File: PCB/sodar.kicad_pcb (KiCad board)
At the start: 2 copper layers, 71 parts, among them J1 Screw_Terminal_01x02, J2 Conn_02x12_Counter_Clockwise, J3 Conn_01x02, U1 TC78H621FNG, U10 TC78H621FNG, U2 TC78H621FNG, U3 TC78H621FNG, U4 TC78H621FNG, U5 TC78H621FNG, U6 TC78H621FNG, U7 TC78H621FNG, U8 TC78H621FNG, U9 TC78H621FNG

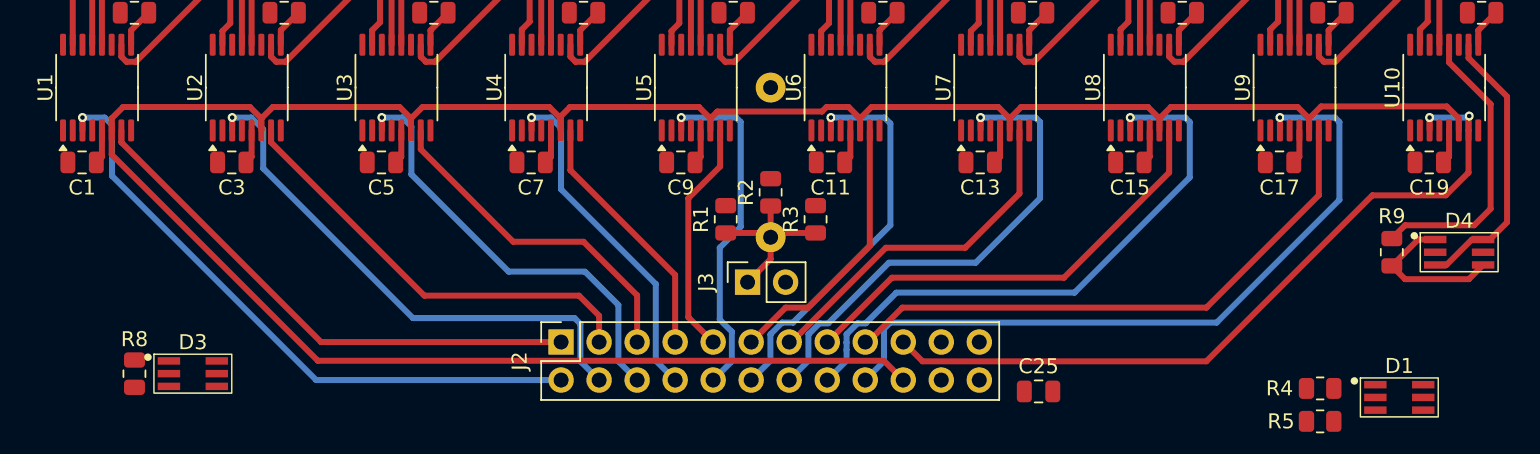
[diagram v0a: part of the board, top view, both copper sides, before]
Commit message: Better STBY routing & Started to route EN
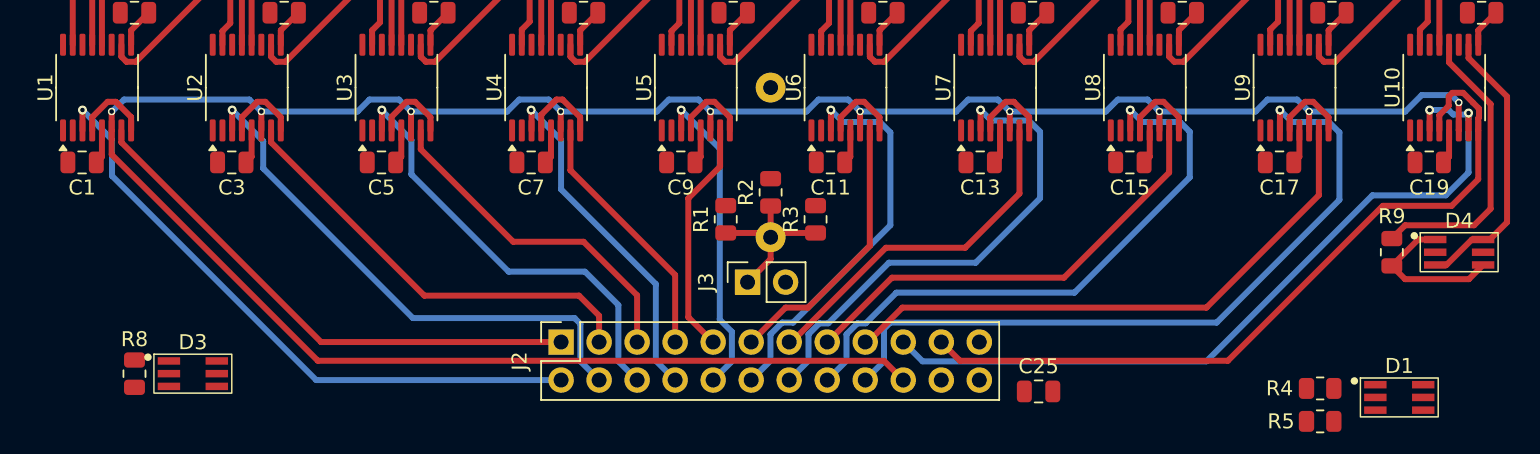
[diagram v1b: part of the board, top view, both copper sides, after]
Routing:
- net EN: track 0.00 -> 98.5 mm
- net STBY: track 165.3 -> 169.9 mm, vias 0 -> 10
- net S9: track 23.7 -> 21.3 mm
- net S19: track 50.9 -> 52.5 mm

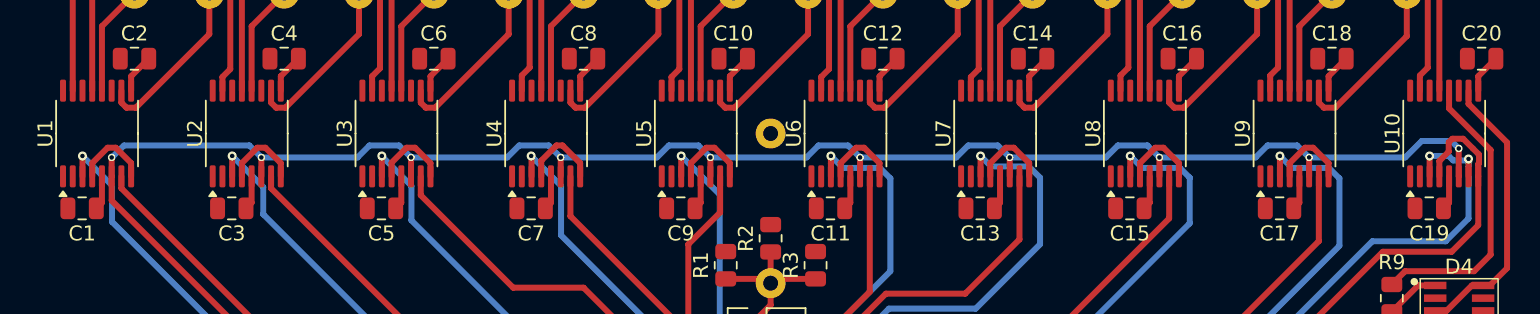
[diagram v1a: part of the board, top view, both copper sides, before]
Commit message: Routed EN
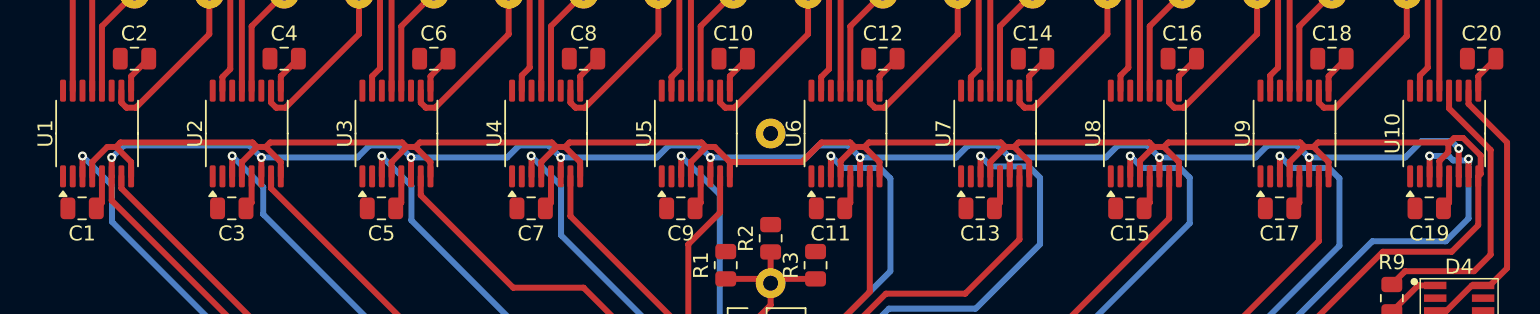
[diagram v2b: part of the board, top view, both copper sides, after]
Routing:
- net EN: track 98.5 -> 185.8 mm

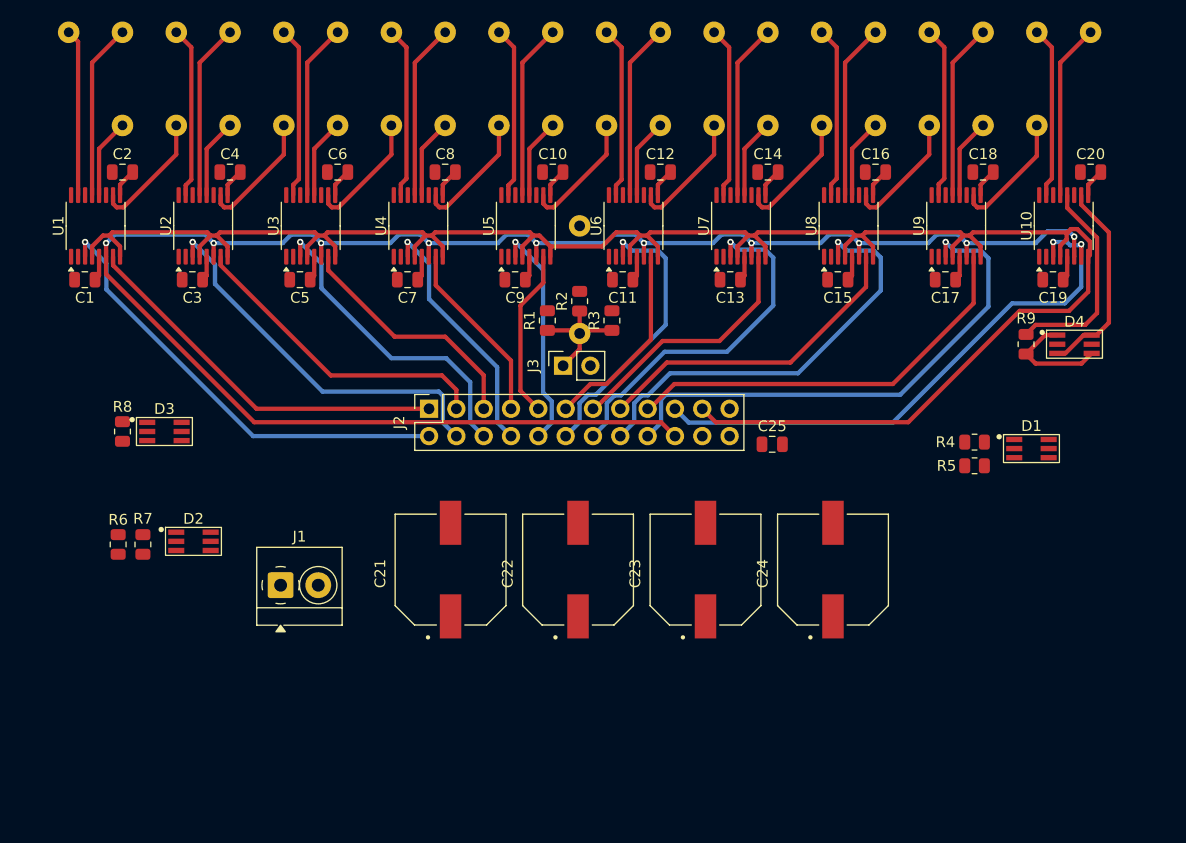
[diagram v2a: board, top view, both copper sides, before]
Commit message: Moved the header 2mm lower so that there is space for the receiver
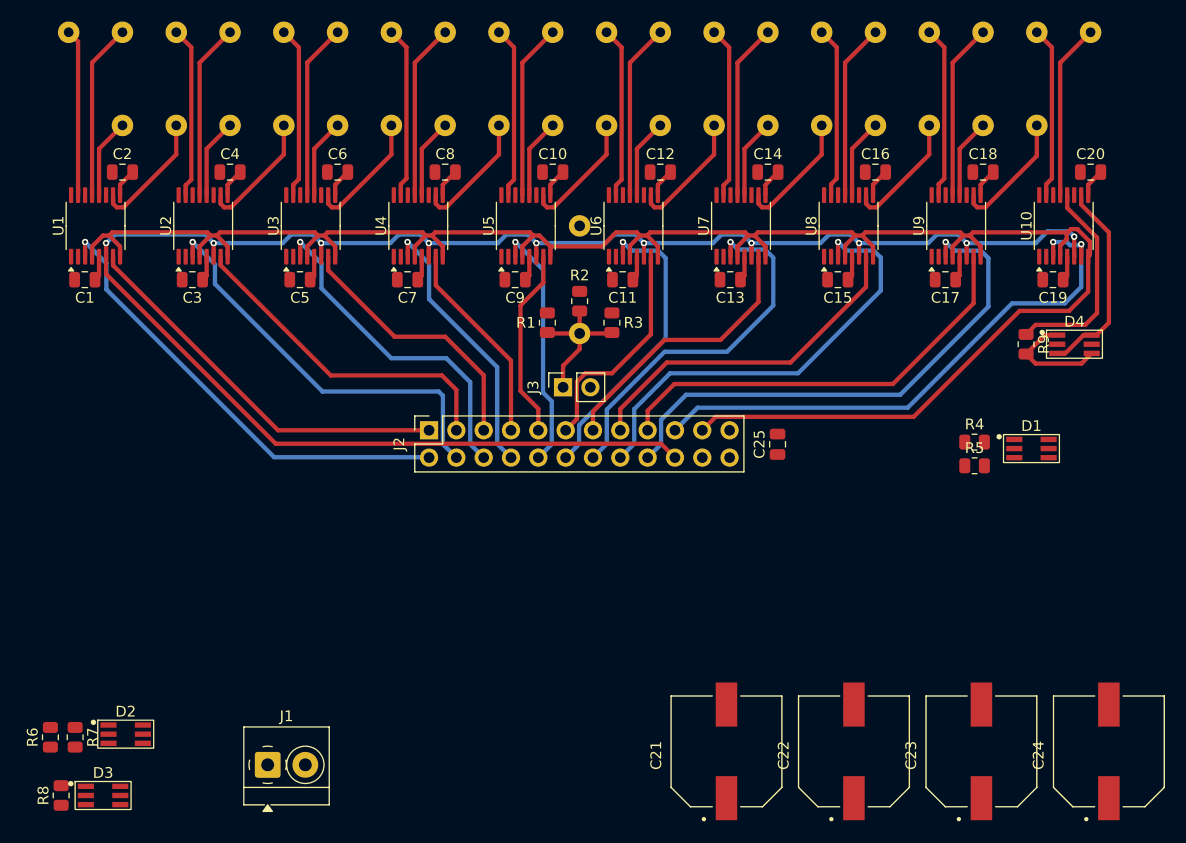
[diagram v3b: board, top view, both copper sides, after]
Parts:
- moved D3 34.3 mm to (105.7, 106.0)
- moved R8 34.3 mm to (101.8, 106.0)
- moved C21 30.7 mm to (163.7, 101.8)
- moved C22 30.7 mm to (175.5, 101.8)
- moved C23 30.7 mm to (187.3, 101.8)
- moved C24 30.7 mm to (199.2, 101.8)
- moved R7 19.0 mm to (103.1, 100.5)
- moved D2 19.0 mm to (107.8, 100.2)
- moved R6 19.0 mm to (100.8, 100.5)
- moved J1 16.7 mm to (121.0, 103.1)
- moved J2 2.00 mm to (136.0, 72.0)
- moved J3 2.00 mm to (148.5, 68.0)
- moved C25 0.50 mm to (168.4, 73.3), turned to 90 degrees
- moved R1 0.20 mm to (147.0, 62.0)
- moved R3 0.20 mm to (153.0, 62.0)
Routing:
- net S12: track 18.3 -> 20.9 mm
- net S5: track 29.3 -> 31.3 mm
- net S10: track 15.7 -> 17.7 mm
- net S9: track 21.3 -> 23.3 mm
- net S8: track 17.0 -> 19.0 mm
- net S6: track 22.9 -> 24.9 mm
- net S4: track 29.3 -> 31.3 mm
- net S3: track 35.9 -> 37.9 mm
- net S7: track 23.4 -> 25.4 mm
- net S16: track 30.3 -> 32.3 mm
- net S18: track 38.7 -> 40.6 mm
- net S14: track 23.7 -> 25.6 mm
- net RX: track 12.0 -> 13.8 mm
- net S15: track 39.9 -> 41.5 mm
- net S13: track 33.2 -> 34.9 mm
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
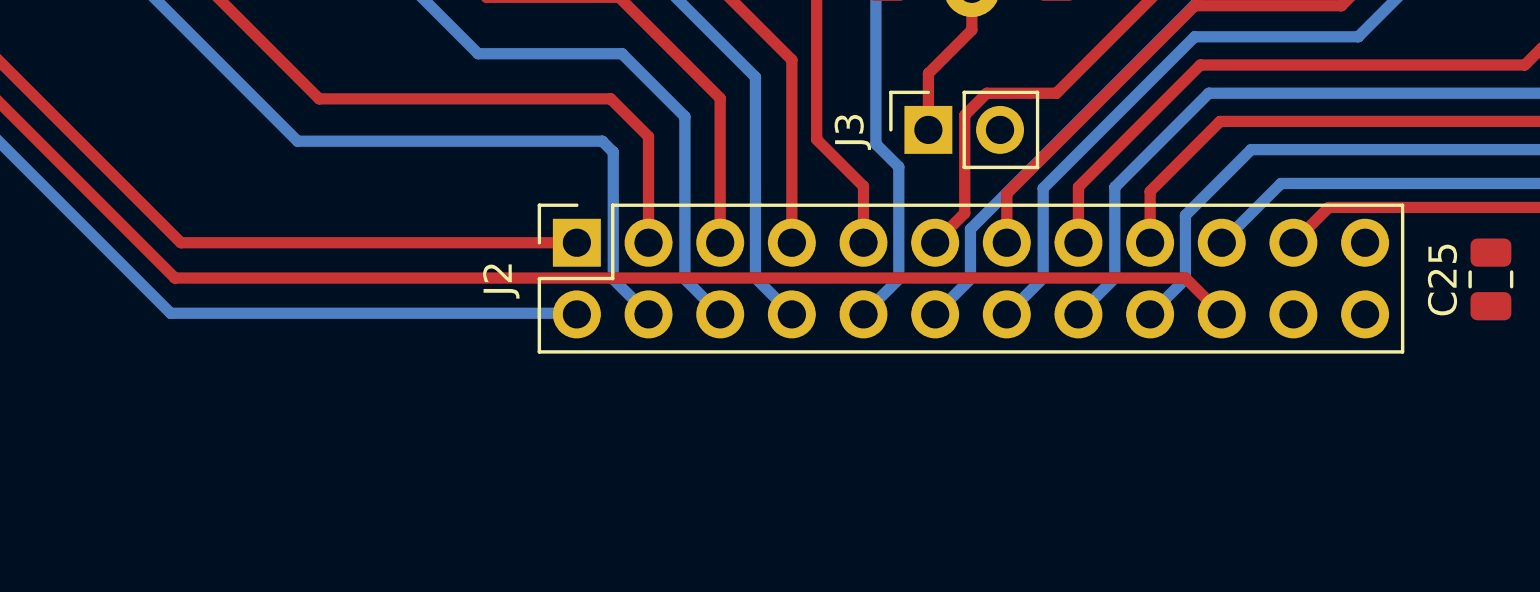
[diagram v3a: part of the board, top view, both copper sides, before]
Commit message: Rerouted STBY to 3V3 as we set it to 3V3 anyway
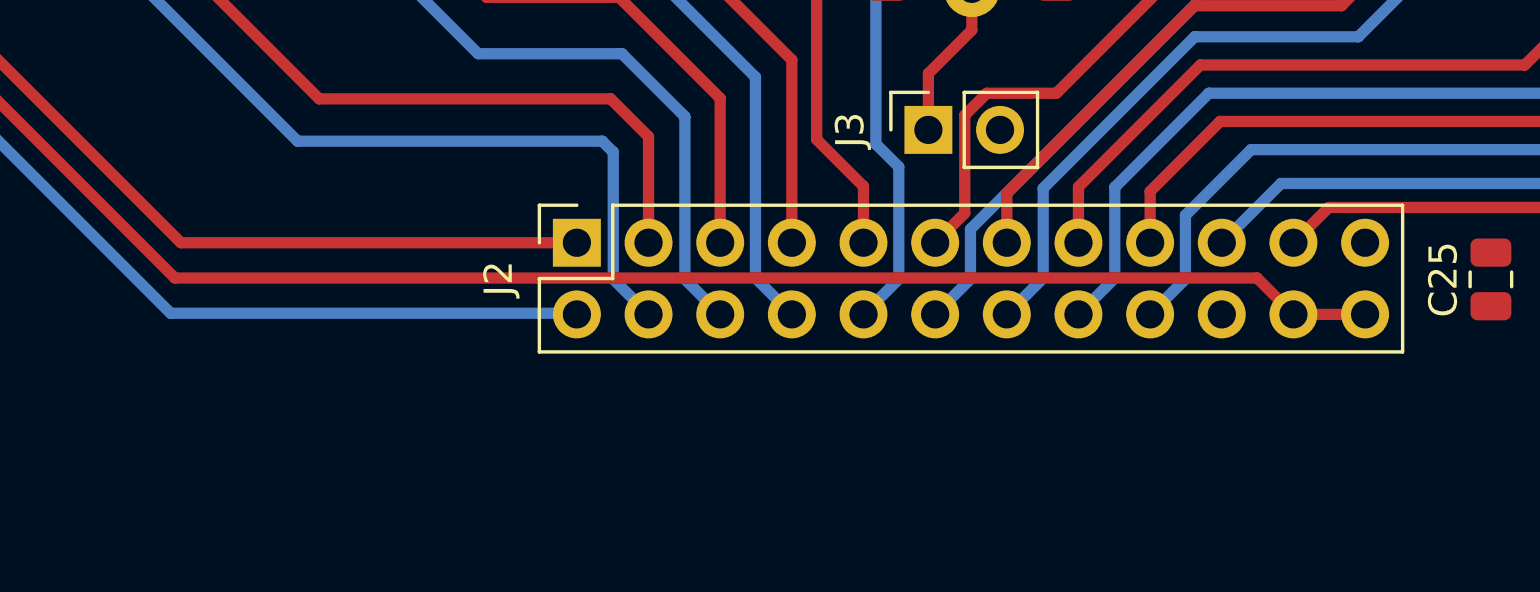
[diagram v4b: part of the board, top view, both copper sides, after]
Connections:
- D1 pad 6: STBY -> +3V3
- J2 pad 20: STBY -> LED
- J2 pad 22: LED -> +3V3
- U1 pad 6: STBY -> +3V3
- U10 pad 6: STBY -> +3V3
- U2 pad 6: STBY -> +3V3
- U3 pad 6: STBY -> +3V3
- U4 pad 6: STBY -> +3V3
- U5 pad 6: STBY -> +3V3
- U6 pad 2: S11 -> unconnected-(U6-NC-Pad2)
- U6 pad 6: STBY -> +3V3
- U7 pad 6: STBY -> +3V3
- U8 pad 6: STBY -> +3V3
- U9 pad 6: STBY -> +3V3
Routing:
- net +3V3: track 22.9 -> 198.8 mm, vias 0 -> 10
- net STBY: track 170.8 -> 0.00 mm, vias 10 -> 0

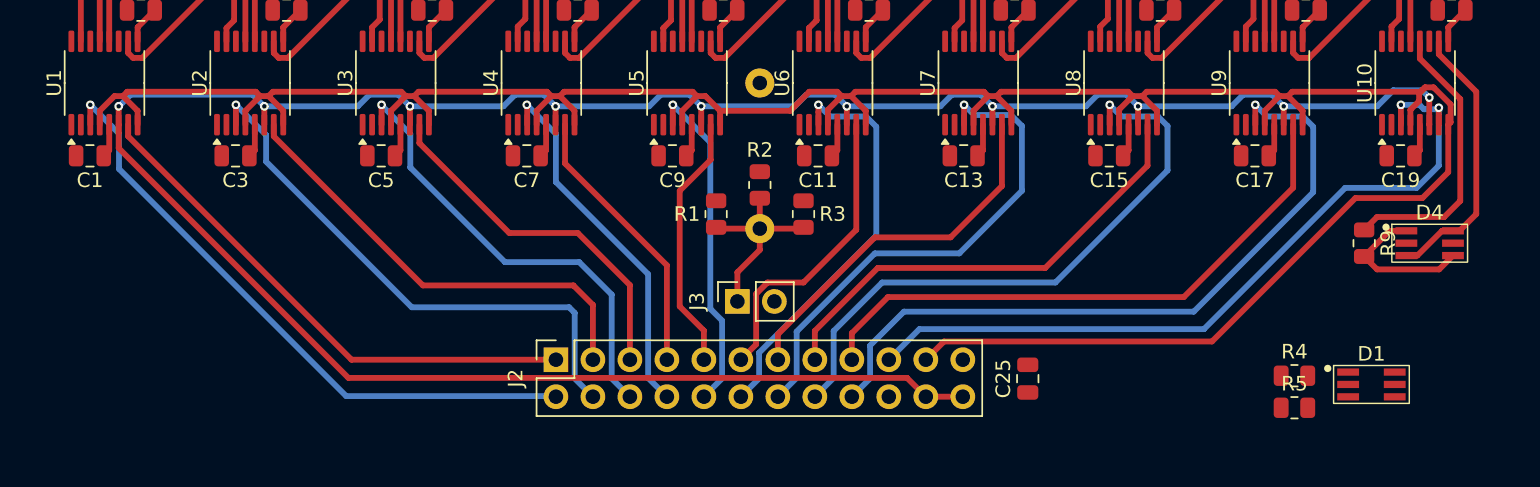
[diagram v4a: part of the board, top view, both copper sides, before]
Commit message: Routed 3V3/STBY
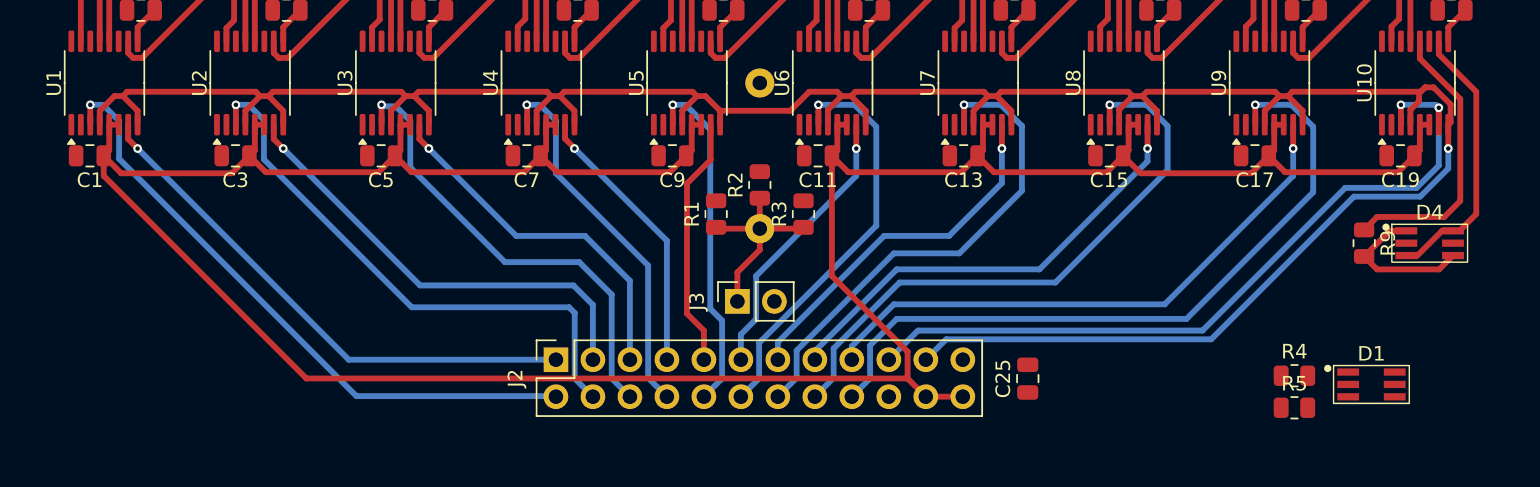
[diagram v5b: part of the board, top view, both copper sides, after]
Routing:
- net +3V3: track 198.8 -> 201.1 mm, vias 10 -> 0
- net S12: track 20.9 -> 19.4 mm, vias 0 -> 1
- net S16: track 32.3 -> 31.3 mm, vias 0 -> 1
- net S18: track 40.6 -> 39.6 mm, vias 0 -> 1
- net S13: track 34.9 -> 34.1 mm
- net S15: track 41.5 -> 40.8 mm
- net S7: track 25.4 -> 25.9 mm
- net S5: track 31.3 -> 31.9 mm
- net S3: track 37.9 -> 38.4 mm
- net S9: track 23.3 -> 23.8 mm
- net S14: track 25.6 -> 25.1 mm, vias 0 -> 1
- net S2: track 36.5 -> 36.7 mm, vias 0 -> 1
- net EN: track 185.6 -> 185.4 mm, vias 0 -> 1
- net S4: track 31.3 -> 31.4 mm, vias 0 -> 1
- net S6: vias 0 -> 1
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
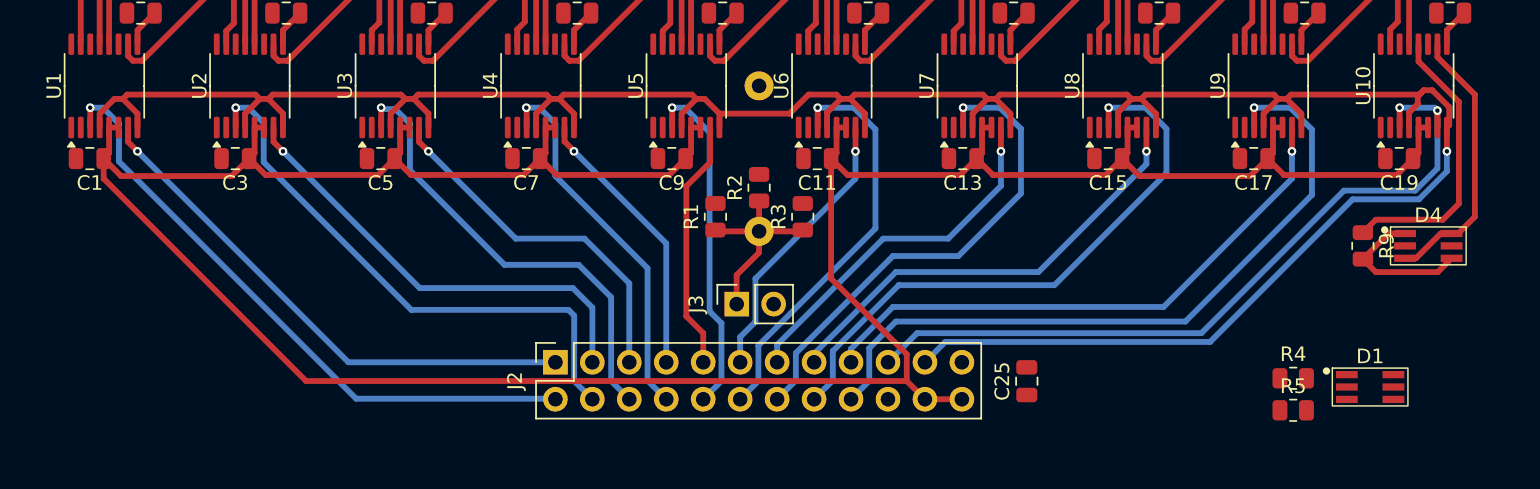
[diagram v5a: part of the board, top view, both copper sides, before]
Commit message: Routed EN on the back for better caps routing
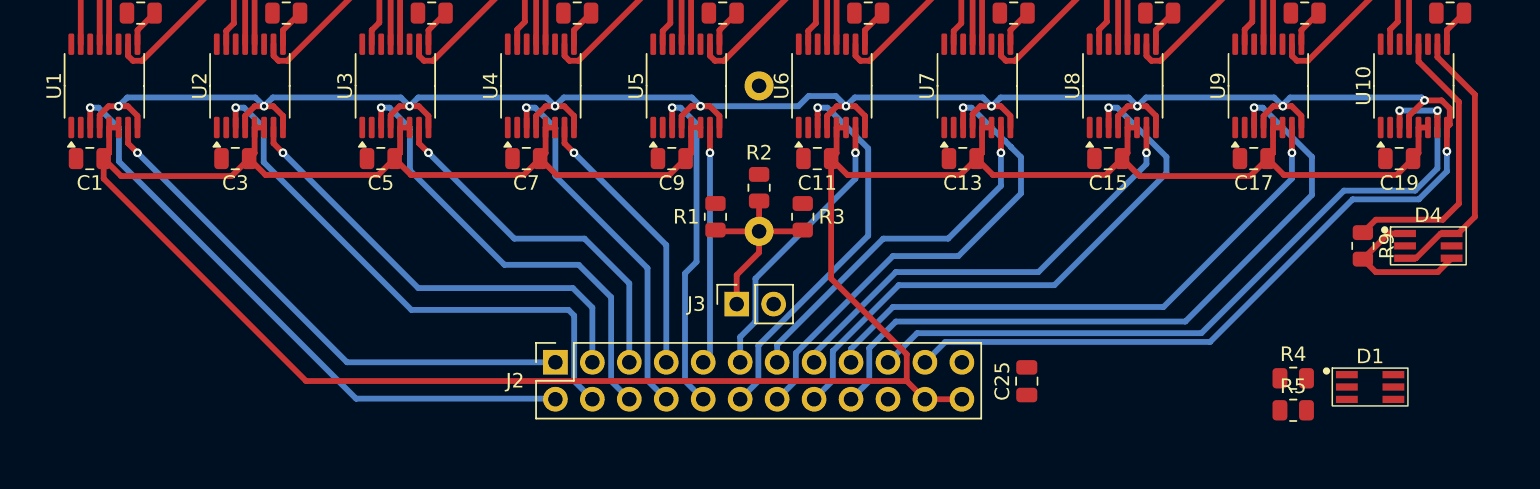
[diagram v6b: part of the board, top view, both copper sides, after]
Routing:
- net EN: track 185.4 -> 186.9 mm, vias 1 -> 11
- net S11: track 28.4 -> 26.9 mm
- net S15: track 40.8 -> 39.7 mm
- net S13: track 34.1 -> 33.0 mm
- net S17: track 49.3 -> 48.2 mm
- net S10: track 17.3 -> 16.2 mm, vias 0 -> 1
- net S9: track 23.8 -> 23.3 mm
